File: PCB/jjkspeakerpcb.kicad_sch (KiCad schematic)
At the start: 19 parts, among them J1 TFT 8PIN, SW1 UP, SW2 DOWN, SW3 TIME SET, SW4 CLOCK SET, SW5 SNOOZE, SW6 ALARM ON, U1 XIAO ESP32-C3

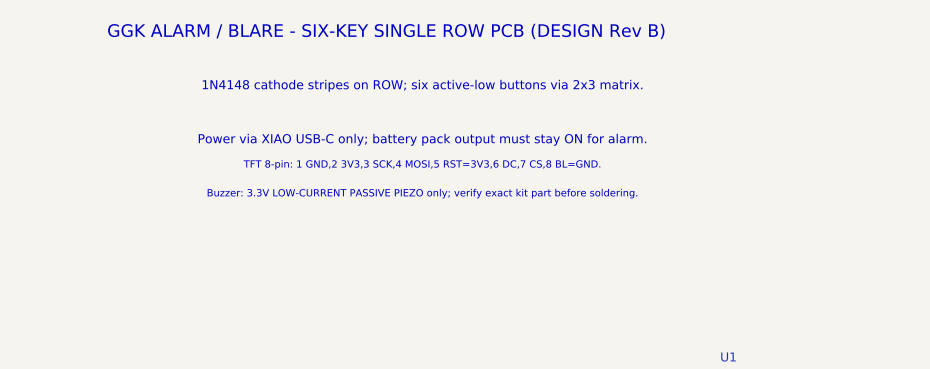
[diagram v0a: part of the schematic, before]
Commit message: Repair malformed GND zone syntax and correct 1N4148 schematic orientation note
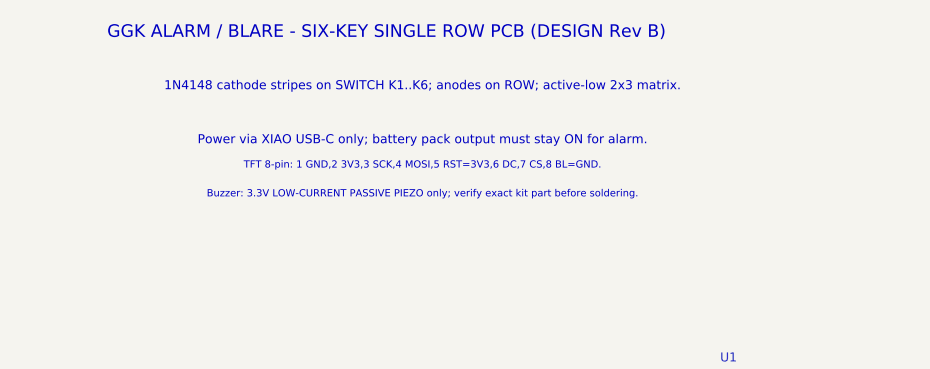
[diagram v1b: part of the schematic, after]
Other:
- note added: "1N4148 cathode stripes on SWITCH K1..K6; anodes on ROW; active-low 2x3 matrix."
- note removed: "1N4148 cathode stripes on ROW; six active-low buttons via 2x3 matrix."
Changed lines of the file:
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@@
 (text "GGK ALARM / BLARE - SIX-KEY SINGLE ROW PCB (DESIGN Rev B)"
    (at 44 21 0) (effects (font (size 1.4 1.4) (thickness .12)) ))
-(text "1N4148 cathode stripes on ROW; six active-low buttons via 2x3 matrix."
+(text "1N4148 cathode stripes on SWITCH K1..K6; anodes on ROW; active-low 2x3 matrix."
    (at 48 27 0) (effects (font (size 1 1) (thickness .12)) ))
 (text "Power via XIAO USB-C only; battery pack output must stay ON for alarm."

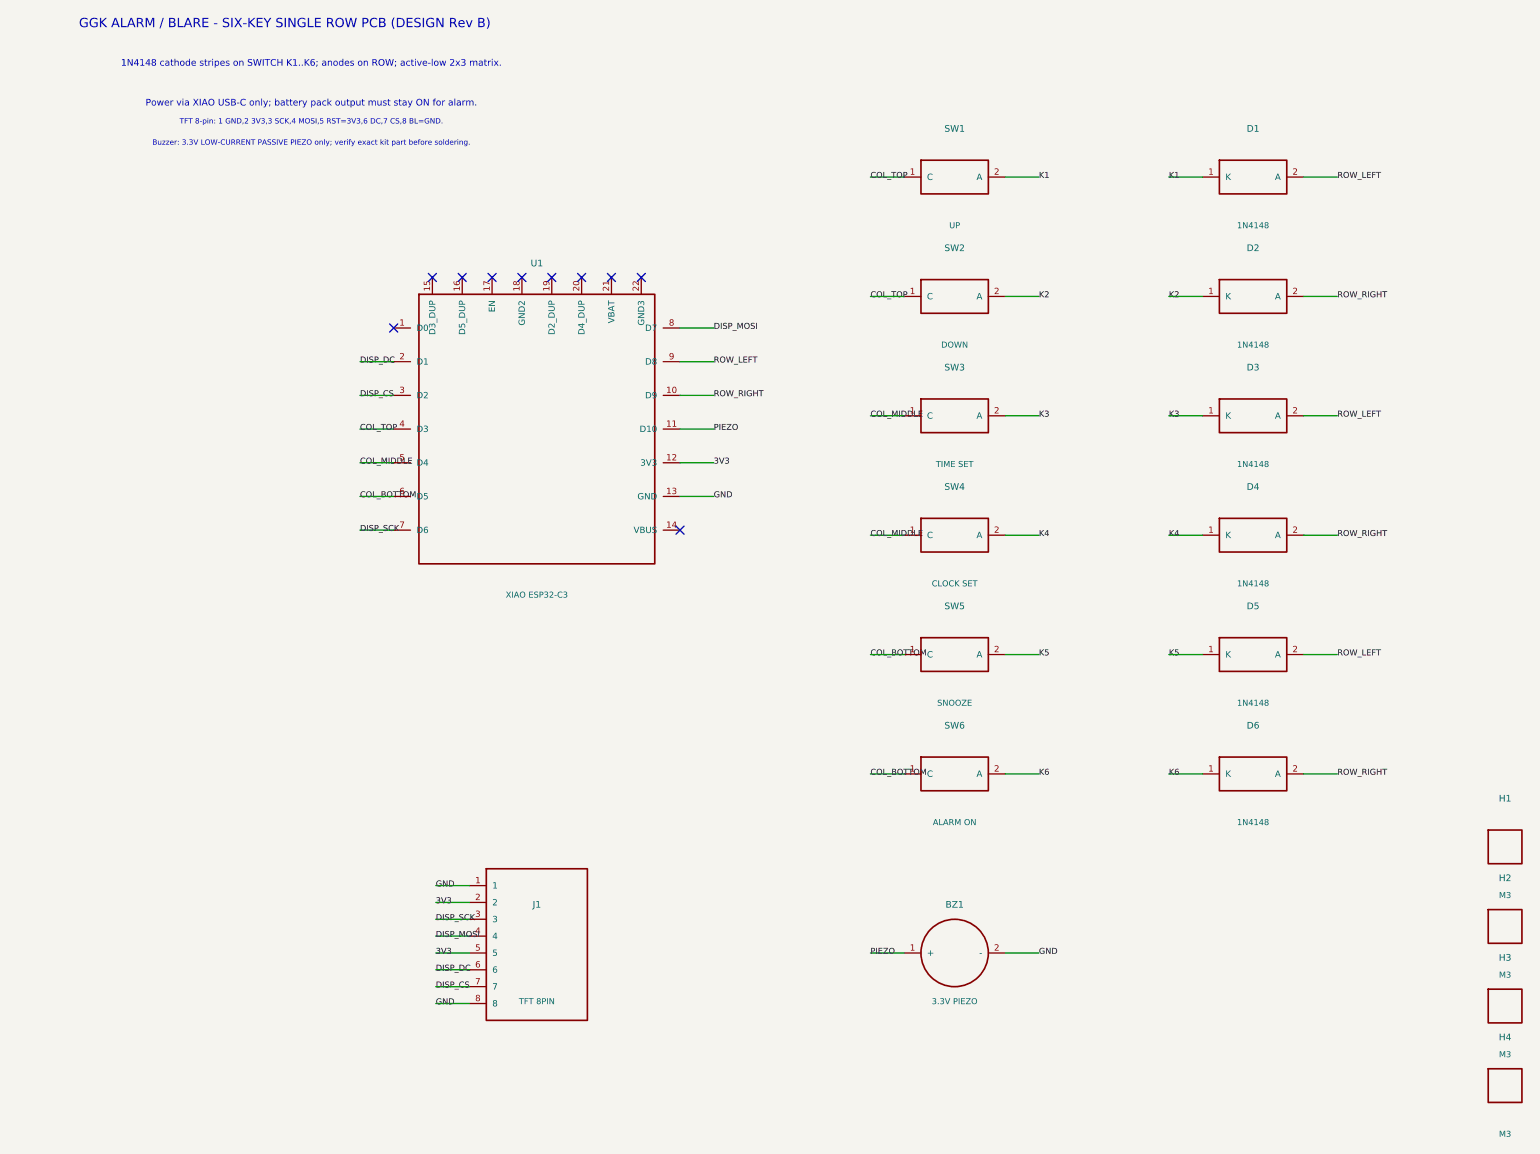
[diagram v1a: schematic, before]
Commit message: Regenerate PCB and schematic using KiCad backside coordinates
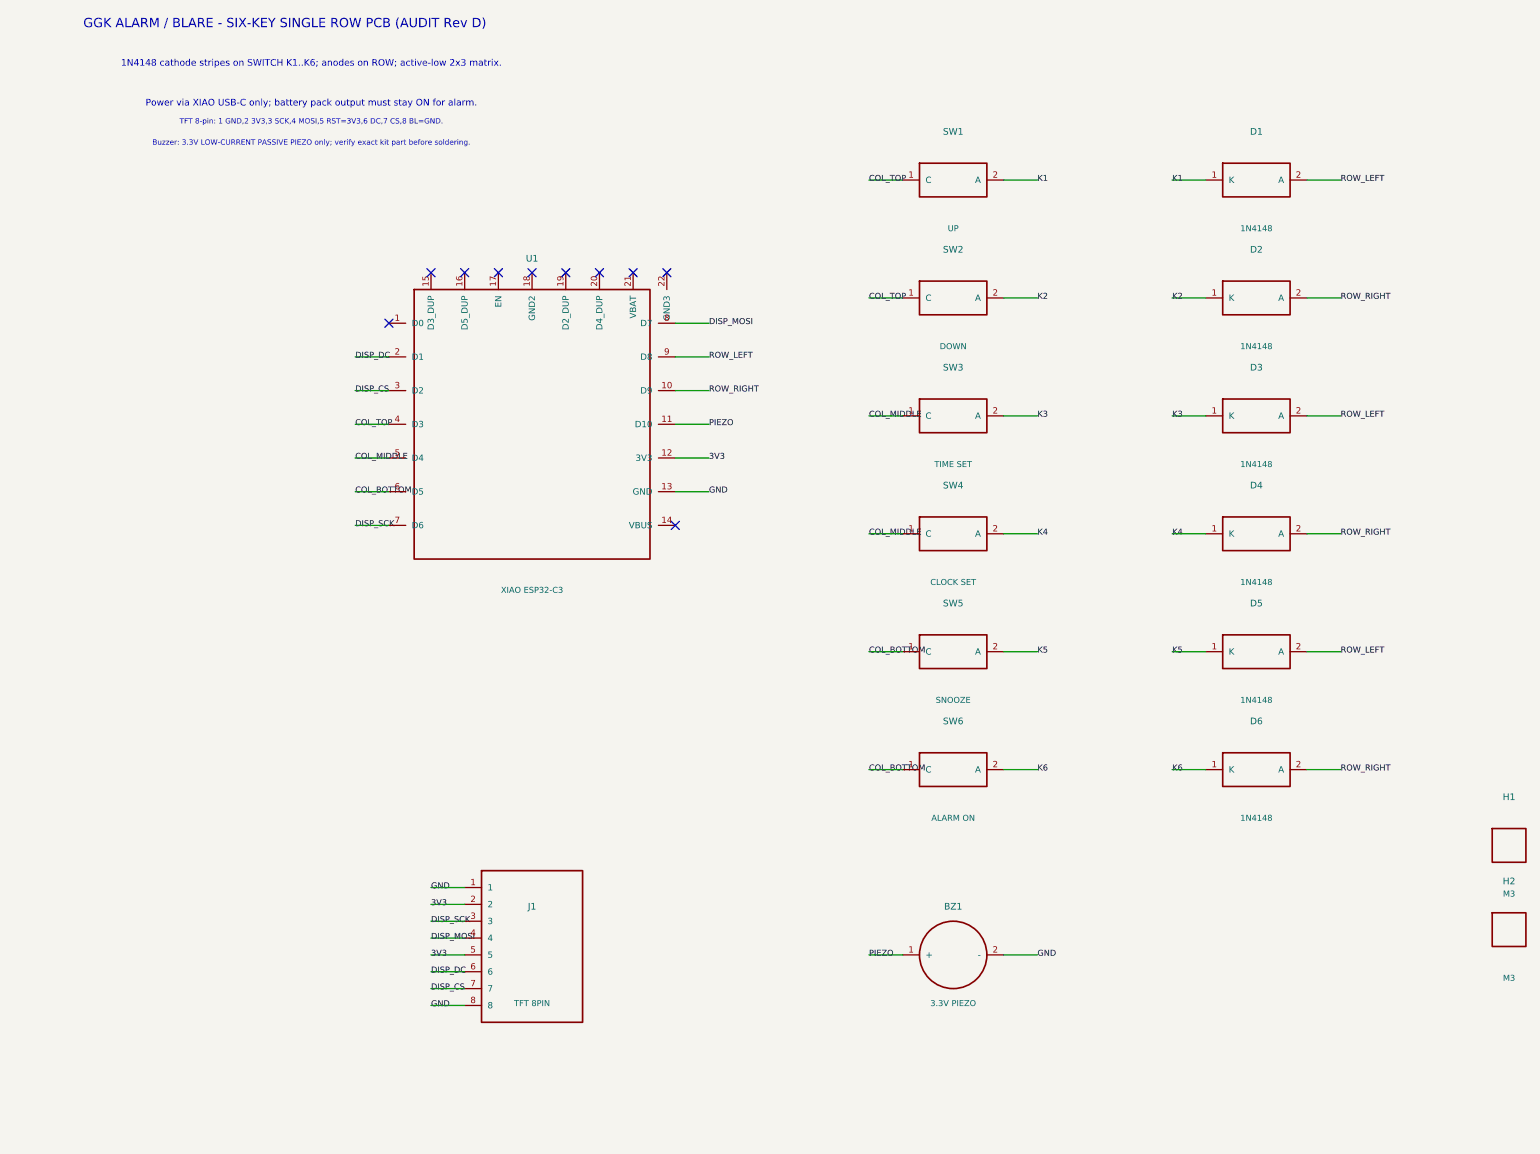
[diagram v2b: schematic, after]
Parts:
- removed H3, H4: M3, GGK:MountingHole_3.2, symbol GGK:M3_MOUNT
- H1, H2: now left out of the parts list
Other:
- note added: "GGK ALARM / BLARE - SIX-KEY SINGLE ROW PCB (AUDIT Rev D)"
- note removed: "GGK ALARM / BLARE - SIX-KEY SINGLE ROW PCB (DESIGN Rev B)"
- moved on the sheet: D1, D2, D3, D4, D5, D6, H1, H2, J1, SW1, SW6, U1
